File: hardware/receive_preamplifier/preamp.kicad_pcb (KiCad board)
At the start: 2 copper layers, 40 x 24 mm, 24 parts, among them J1 RF_IN, J2 RF_OUT, J3 Power, U1 PHA-13LN, U2 7805

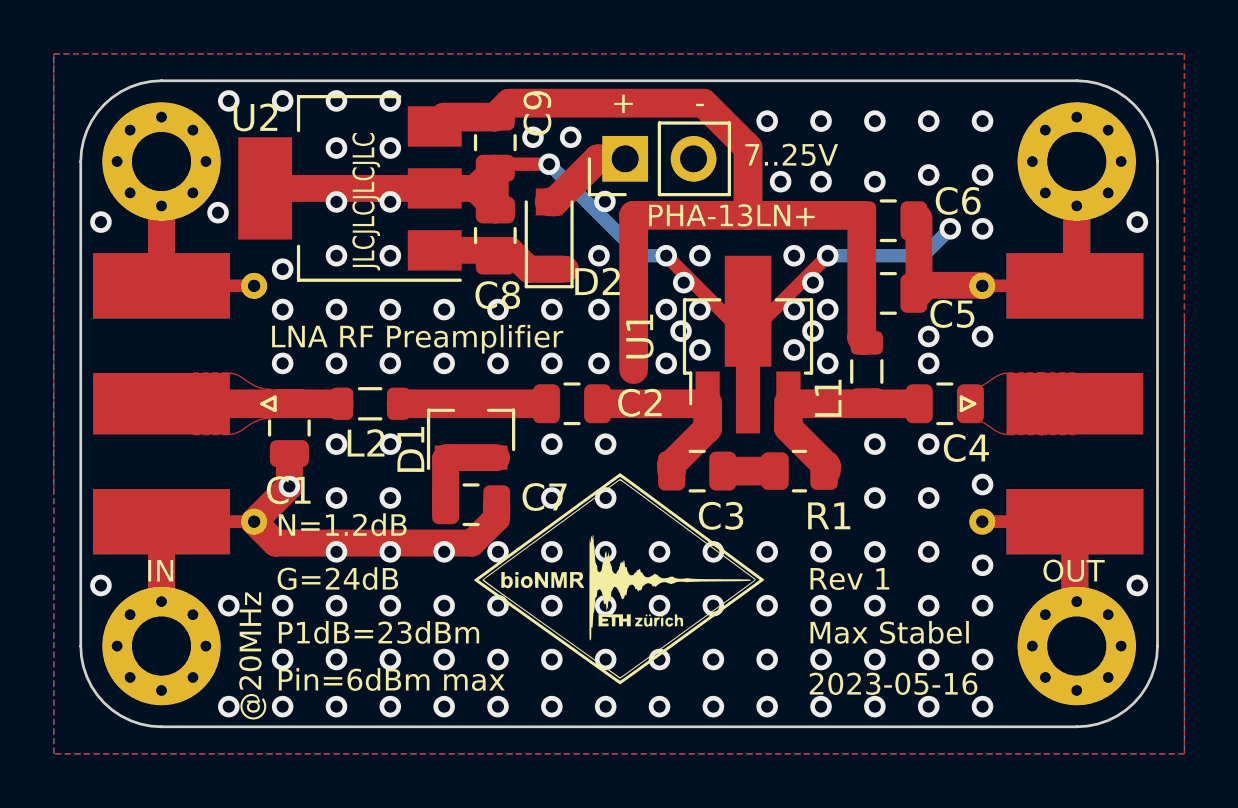
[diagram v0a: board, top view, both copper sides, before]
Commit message: Fix lna feedback loop
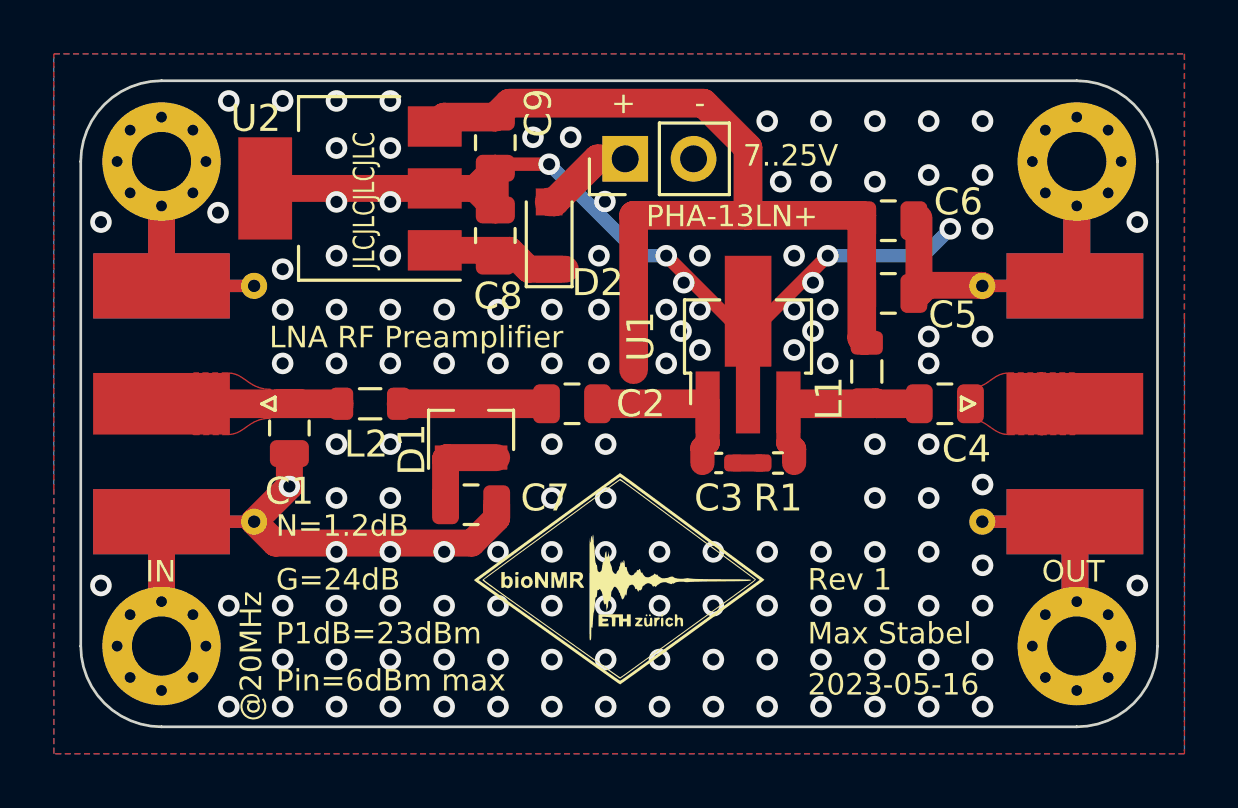
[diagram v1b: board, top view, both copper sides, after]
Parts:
- C3: footprint Capacitor_SMD:C_0805_2012Metric -> Capacitor_SMD:C_0402_1005Metric_Pad0.74x0.62mm_HandSolder
- R1: footprint Resistor_SMD:R_0805_2012Metric -> Resistor_SMD:R_0402_1005Metric_Pad0.72x0.64mm_HandSolder
- moved C3 0.85 mm to (155.3, 96.4)
- moved R1 0.85 mm to (157.5, 96.4)
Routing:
- net /rf_lna_out: track 7.17 -> 6.37 mm
- net /rf_lna_in: track 6.85 -> 6.08 mm
- net Net-(C3-Pad2): track 1.76 -> 1.03 mm
